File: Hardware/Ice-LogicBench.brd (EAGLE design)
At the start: 121 x 100 mm, 106 parts, among them IC1 S27KL0641DABHV020, IC2 S26KL128SDABHI020, IC3 USBLC6-2SC6, IC4 ICE40HX4K-BG121, IC5 FUSB302MPX, IC6 USBLC6-2SC6, J2 QWIIC_RIGHT_ANGLE, Y3 12MZ

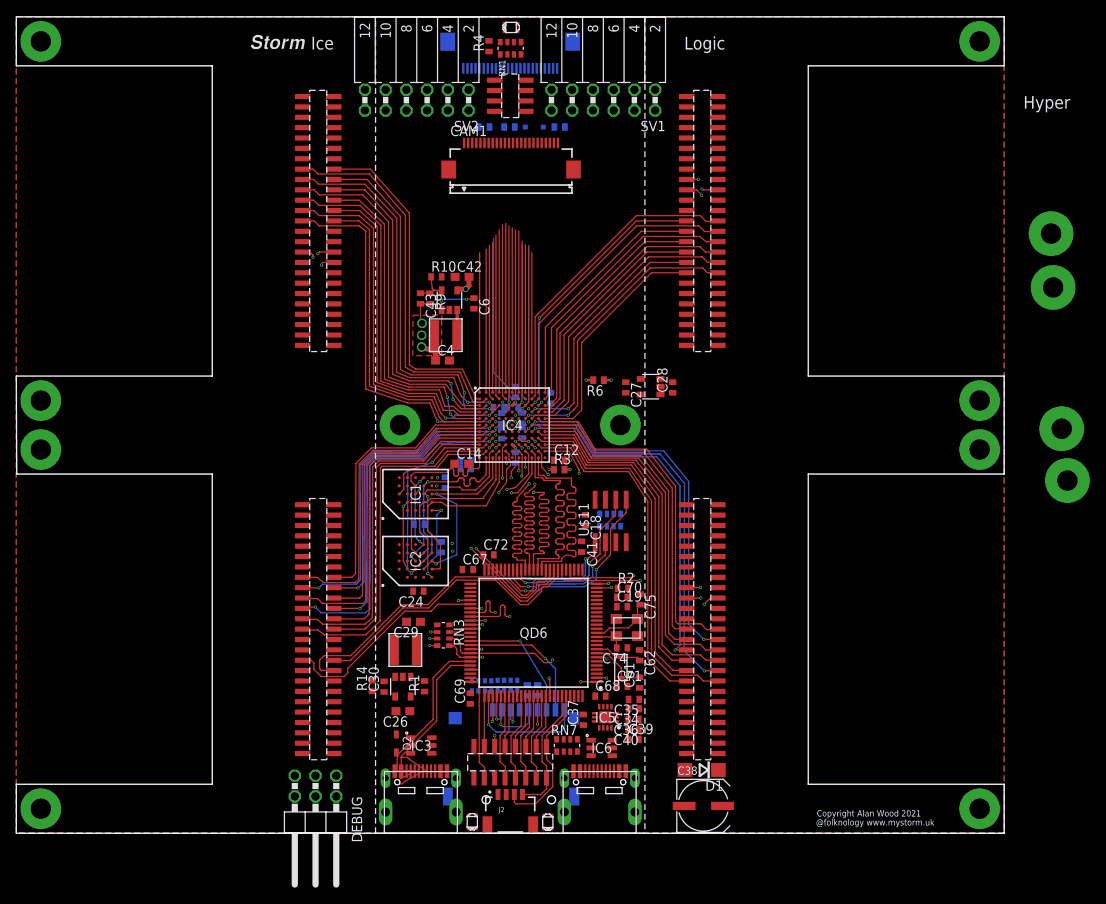
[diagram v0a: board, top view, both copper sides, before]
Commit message: Added readme tile link
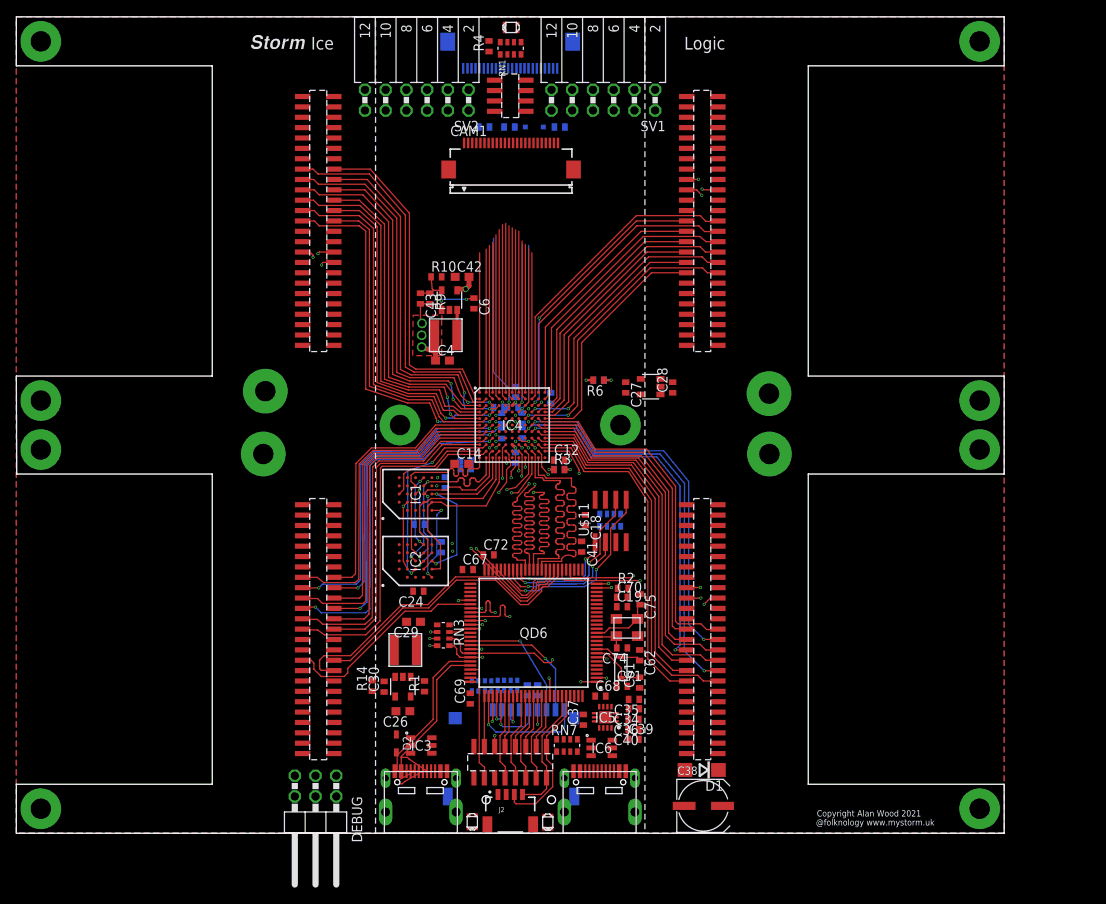
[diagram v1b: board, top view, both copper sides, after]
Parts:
- moved H1 98.6 mm to (30.2, 46.5)
- moved H2 97.7 mm to (30.5, 54.1)
- moved H3 40.3 mm to (92.2, 46.5)
- moved H4 39.7 mm to (92.2, 53.9)
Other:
- board text removed: "Bench"
- board text removed: "Hyper"
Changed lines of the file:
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@@
 <text x="97.95" y="0.95" size="0.77" layer="21">@folknology www.mystorm.uk</text>
 <text x="73.8" y="-2.55" size="1.778" layer="39">Redo messed up 0402 pad sizes</text>
-<text x="131.25" y="84.45" size="1.55" layer="29" font="vector" ratio="14">Bench</text>
 <text x="81.8" y="96" size="1.55" layer="21" font="vector" ratio="14">Logic</text>
 <text x="36.1" y="96" size="1.55" layer="21" font="vector" ratio="14">Ice</text>
 <text x="88.7" y="96" size="1.55" layer="29" font="vector" ratio="14">Deck</text>
-<text x="123.35" y="88.75" size="1.55" layer="21" font="vector" ratio="14">Hyper</text>
 <text x="98.05" y="2.05" size="0.77" layer="21">Copyright Alan Wood 2021</text>
 </plain>
@@
 <attribute name="MANUFACTURER_NAME" value="Lattice Semiconductor" x="60.75" y="50" size="1.778" layer="27" display="off"/>
 </element>
-<element name="H1" library="amino" package="2M5-LARGE" value="HOLE2.5MM-LARGE" x="128.75" y="43.2"/>
-<element name="H2" library="amino" package="2M5-LARGE" value="HOLE2.5MM-LARGE" x="128.05" y="49.55"/>
-<element name="H3" library="amino" package="2M5-LARGE" value="HOLE2.5MM-LARGE" x="127" y="66.85"/>
-<element name="H4" library="amino" package="2M5-LARGE" value="HOLE2.5MM-LARGE" x="126.75" y="73.45"/>
+<element name="H1" library="amino" package="2M5-LARGE" value="HOLE2.5MM-LARGE" x="30.25" y="46.45"/>
+<element name="H2" library="amino" package="2M5-LARGE" value="HOLE2.5MM-LARGE" x="30.5" y="54.15"/>
+<element name="H3" library="amino" package="2M5-LARGE" value="HOLE2.5MM-LARGE" x="92.25" y="46.45"/>
+<element name="H4" library="amino" package="2M5-LARGE" value="HOLE2.5MM-LARGE" x="92.2" y="53.85"/>
 <element name="C1" library="rcl" package="C0402" value="470nf" x="55.05" y="44.65" rot="MR180"/>
 <element name="C2" library="rcl" package="C0402" value="470nf" x="59.1" y="52.15" rot="MR0"/>
@@
 <contactref element="U$30" pad="P$47"/>
 <contactref element="MEZZANINE" pad="V+"/>
-<wire x1="128.05" y1="49.55" x2="126.75" y2="73.45" width="0" layer="19" extent="1-1"/>
-<wire x1="85.925" y1="83.89" x2="126.75" y2="73.45" width="0" layer="19" extent="1-1"/>
+<wire x1="30.5" y1="54.15" x2="92.2" y2="53.85" width="0" layer="19" extent="1-1"/>
+<wire x1="85.925" y1="83.89" x2="92.2" y2="53.85" width="0" layer="19" extent="1-1"/>
 <wire x1="85.925" y1="85.16" x2="85.925" y2="83.89" width="0" layer="19" extent="1-1"/>
 <wire x1="85.925" y1="86.43" x2="85.925" y2="85.16" width="0" layer="19" extent="1-1"/>
@@
 <contactref element="U$30" pad="P$29" route="any" routetag="G$1.V-"/>
 <contactref element="MEZZANINE" pad="V-"/>
-<wire x1="128.75" y1="43.2" x2="127" y2="66.85" width="0" layer="19" extent="1-1"/>
-<wire x1="85.925" y1="66.11" x2="127" y2="66.85" width="0" layer="19" extent="1-1"/>
+<wire x1="30.25" y1="46.45" x2="92.25" y2="46.45" width="0" layer="19" extent="1-1"/>
+<wire x1="85.925" y1="66.11" x2="92.25" y2="46.45" width="0" layer="19" extent="1-1"/>
 <wire x1="47" y1="50" x2="82.115" y2="59.76" width="0" layer="19" extent="1-1"/>
 <wire x1="38.885" y1="40.24" x2="47" y2="50" width="0" layer="19" extent="1-1"/>

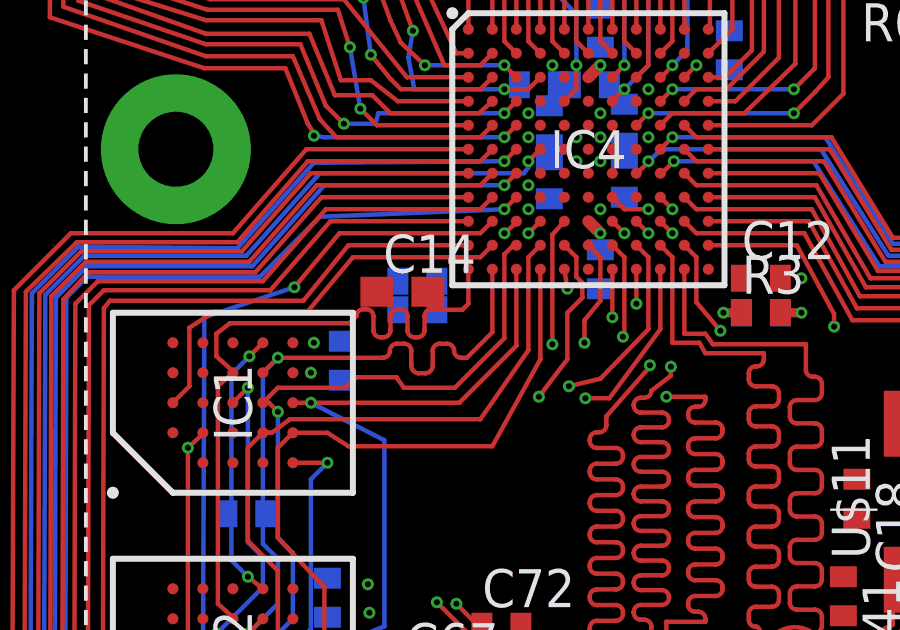
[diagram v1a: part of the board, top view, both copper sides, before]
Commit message: Juggled some pins to improve IO frm @tnt suggestion
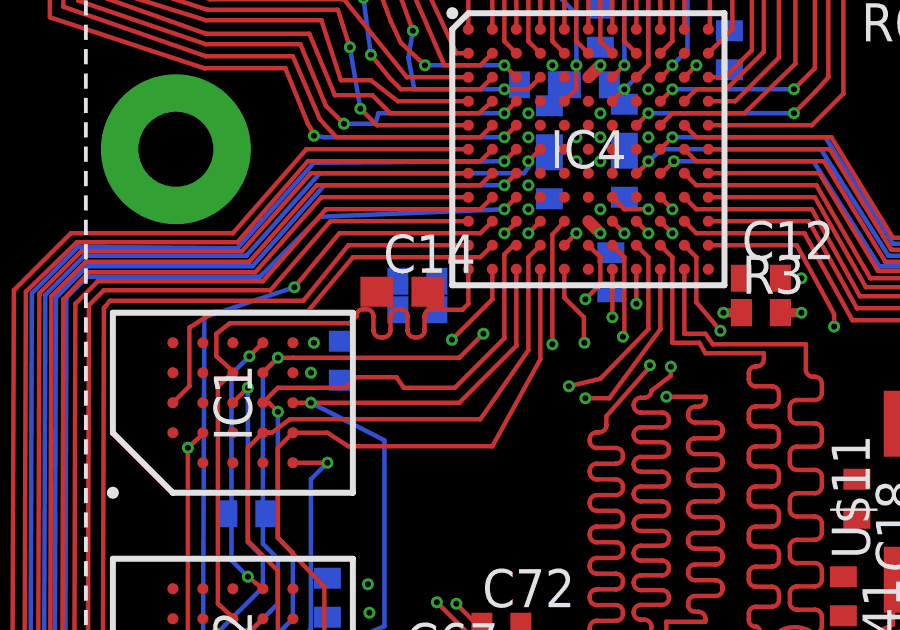
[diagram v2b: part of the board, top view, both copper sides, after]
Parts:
- moved C16 0.36 mm to (61.5, 45.9)
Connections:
- new net GPLL0: C13.1, C16.1, IC4.L6
- new net GPLL1: C15.1, C17.1, IC4.C5
- net CLK: now also IC4.L5; no longer IC4.K6
- net DQ3: now also IC4.K5; no longer IC4.L2
- net DQK: now also IC4.L2; no longer IC4.L5
- net G/SDA: now also IC4.A6; no longer IC4.B6
- net GND: no longer C13.1, C15.1, C16.1, C17.1, IC4.C5, IC4.L6
- net R/SCL: now also IC4.B6; no longer IC4.A6
- net TX: now also IC4.K6; no longer IC4.K5
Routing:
- net DQ3: track 22.8 -> 24.6 mm, vias 2 -> 4
- net DQK: track 23.2 -> 21.8 mm
- net R/SCL: track 20.2 -> 21.4 mm
- net G/SDA: track 21.4 -> 20.2 mm
- net CLK: track 28.9 -> 27.9 mm

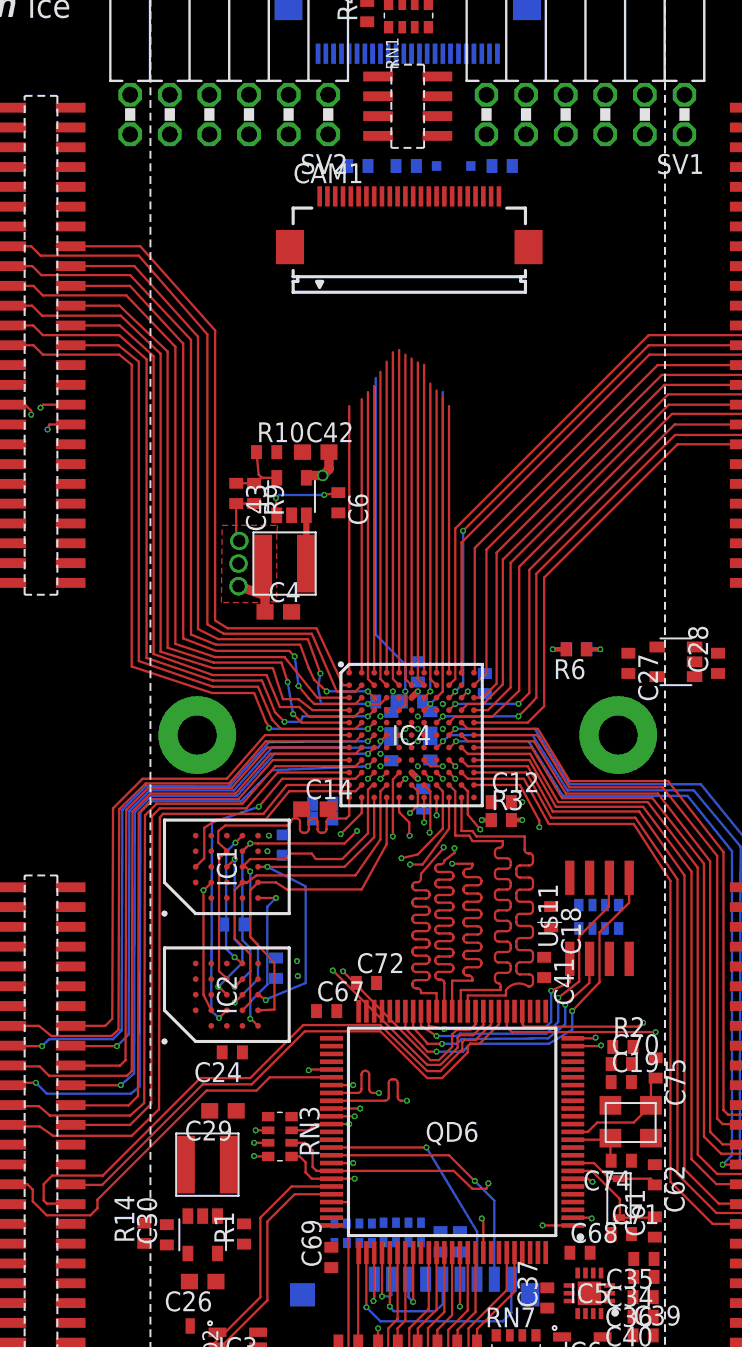
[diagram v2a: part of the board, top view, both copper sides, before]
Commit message: Added series resistors for fast data lines and a cs jumper to alloy hyperflash to be swapped by 2nd hyperram
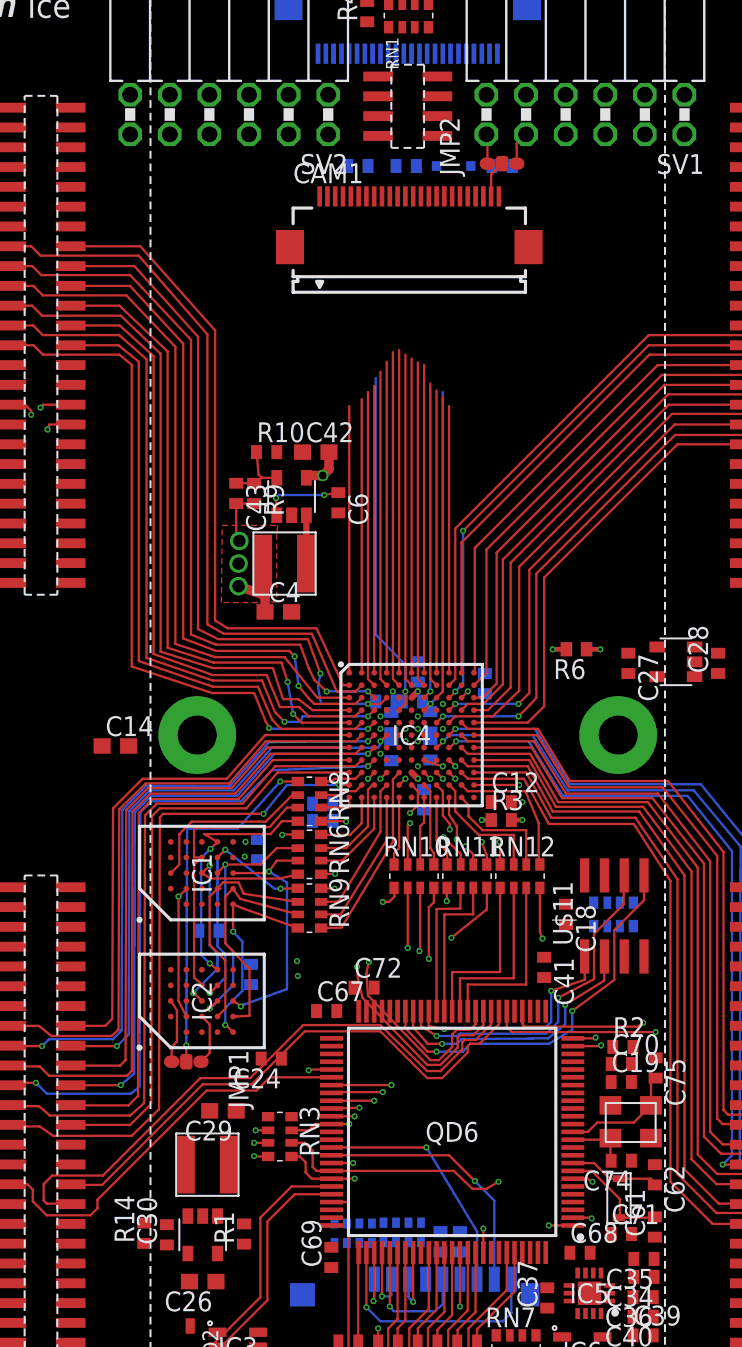
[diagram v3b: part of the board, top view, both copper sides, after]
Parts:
- added JMP1, JMP2: 0R-JUMPC, jump-0r-smd:C0R-JMP
- added RN10, RN11, RN12, RN6, RN8, RN9: 22r, resistor-dil:EXB38V
- moved C14 13.4 mm to (41.8, 49.3)
- moved C24 2.53 mm to (51.8, 29.2)
- moved C22 1.68 mm to (50.9, 42.6)
- moved C25 1.65 mm to (47.8, 37.5)
- moved IC1 1.65 mm to (47.3, 41.1)
- moved IC2 1.65 mm to (47.3, 33.0)
- moved C23 1.65 mm to (50.5, 34.6)
- moved C18 0.96 mm to (70.7, 38.5)
- moved RN4 0.96 mm to (73.7, 38.5)
- moved U$11 0.96 mm to (73.8, 38.4)
- moved C72 0.34 mm to (57.7, 33.8)
- moved C1 0.15 mm to (55.0, 44.5)
- moved C16 0.07 mm to (61.5, 45.9)
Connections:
- new net !QSSX: IC4.K10, RN12.5
- new net CLKX: IC4.L5, RN10.8
- new net DQ0X: IC4.K3, RN6.7
- new net DQ1X: IC4.K4, RN9.7
- new net DQ2X: IC4.L1, RN8.6
- new net DQ3X: IC4.K5, RN9.8
- new net DQ4X: IC4.J3, RN8.5
- new net DQ5X: IC4.L3, RN6.6
- new net DQ6X: IC4.L4, RN9.6
- new net DQ7X: IC4.J5, RN9.5
- new net DQKX: IC4.L2, RN6.8
- new net DQRX: IC4.J4, RN6.5
- new net DS0X: IC4.J2, RN8.8
- new net DS1X: IC4.K2, RN8.7
- new net DSF: IC2.C2, JMP1.1
- new net DSR: IC2.A3, JMP1.3
- new net N$26: CAM1.23, JMP2.2
- new net QCKX: IC4.L10, RN12.6
- new net QD0X: IC4.K9, RN12.7
- new net QD1X: IC4.J9, RN12.8
- new net QD2X: IC4.J8, RN11.6
- new net QD3X: IC4.H7, RN11.7
- new net QD4X: IC4.L7, RN10.6
- new net QD5X: IC4.K7, RN10.5
- new net QD6X: IC4.L8, RN11.8
- new net QD7X: IC4.H9, RN11.5
- new net QDRX: IC4.J7, RN10.7
- net !QSS: now also RN12.4; no longer IC4.K10
- net +3V3: now also IC4.L11, JMP2.1
- net CLK: now also RN10.1; no longer IC4.L5
- net DQ0: now also RN6.2; no longer IC4.K3
- net DQ1: now also RN9.2; no longer IC4.K4
- net DQ2: now also RN8.3; no longer IC4.L1
- net DQ3: now also RN9.1; no longer IC4.K5
- net DQ4: now also RN8.4; no longer IC4.J3
- net DQ5: now also RN6.3; no longer IC4.L3
- net DQ6: now also RN9.3; no longer IC4.L4
- net DQ7: now also RN9.4; no longer IC4.J5
- net DQK: now also RN6.1; no longer IC4.L2
- net DQR: now also RN6.4; no longer IC4.J4
- net DS0: now also JMP1.2, RN8.1; no longer IC2.C2, IC4.J2
- net DS1: now also RN8.2; no longer IC4.K2
- net GND: now also CAM1.24, JMP2.3; no longer CAM1.23
- net QCK: now also RN12.3; no longer IC4.L10
- net QD0: now also RN12.2; no longer IC4.K9
- net QD1: now also RN12.1; no longer IC4.J9
- net QD2: now also RN11.3; no longer IC4.J8
- net QD3: now also RN11.2; no longer IC4.H7
- net QD4: now also RN10.3; no longer IC4.L7
- net QD5: now also RN10.4; no longer IC4.K7
- net QD6: now also RN11.1; no longer IC4.L8
- net QD7: now also RN11.4; no longer IC4.H9
- net QDR: now also RN10.2; no longer IC4.J7
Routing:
- net QD3: track 29.5 -> 9.41 mm, vias 2 -> 0
- net QD2: track 29.4 -> 9.76 mm, vias 2 -> 0
- net QD1: track 29.5 -> 11.0 mm, vias 2 -> 0
- net QCK: track 29.6 -> 11.7 mm
- net QD0: track 29.3 -> 11.4 mm
- net RX: track 45.9 -> 32.6 mm
- net QDR: track 29.9 -> 16.9 mm
- net DQ7X: track 0.00 -> 12.3 mm
- net QD4: track 30.0 -> 17.9 mm
- net QD5: track 30.1 -> 18.9 mm
- net QD7: track 30.6 -> 20.5 mm
- net DQ3X: track 0.00 -> 10.1 mm, vias 0 -> 2
- net DQ7: track 23.2 -> 13.5 mm, vias 3 -> 2
- net DQ6X: track 0.00 -> 9.59 mm
- net DQ1X: track 0.00 -> 9.50 mm
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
